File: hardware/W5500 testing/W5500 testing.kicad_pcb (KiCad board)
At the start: 2 copper layers, 34.4 x 53.7 mm, 43 parts, among them J4 Conn_01x08_Pin, J5 RJ45_Amphenol_RJMG1BD3B8K1ANR, Q4 MMBT5550L, Q5 MMBT5550L, U22 W5500, Y1 Crystal_GND24

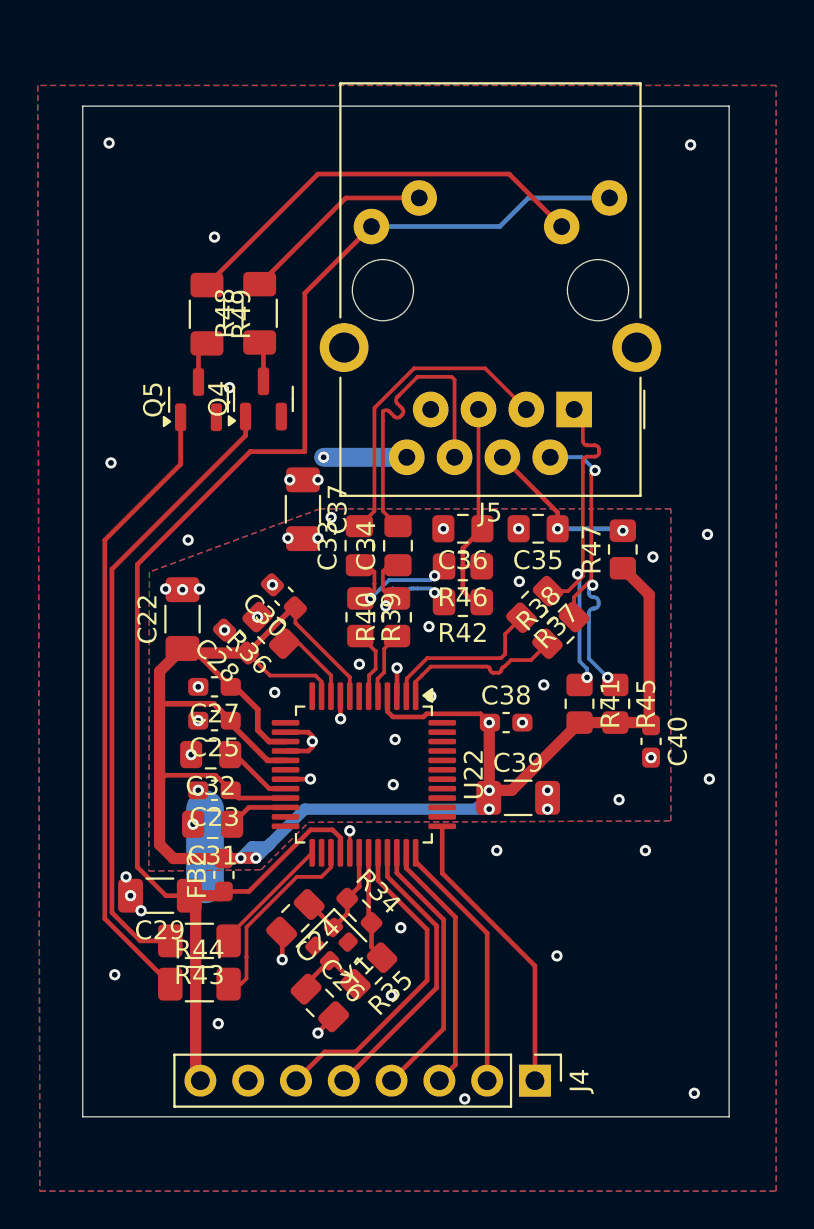
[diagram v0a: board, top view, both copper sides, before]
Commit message: VT interconnect cable specs and w5500 test board
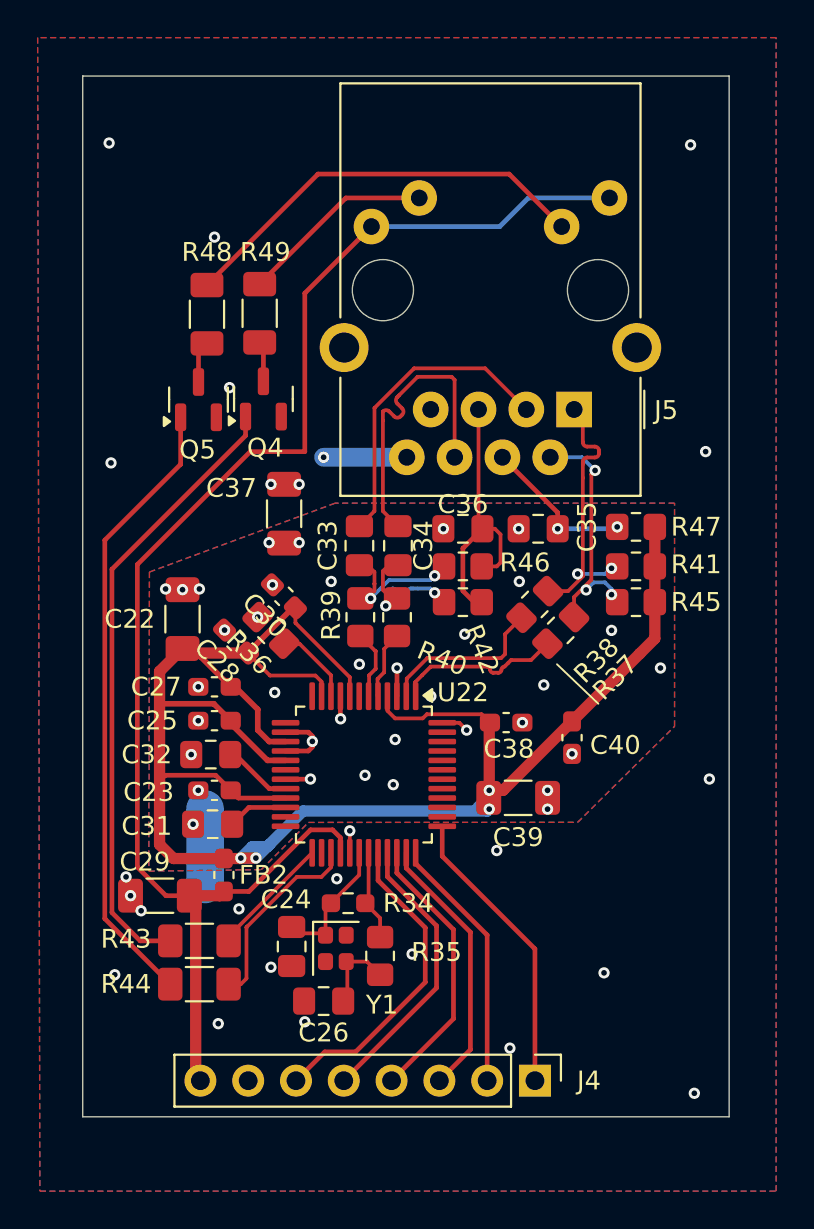
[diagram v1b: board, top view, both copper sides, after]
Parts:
- moved R41 7.89 mm to (134.9, 102.9), turned to 0 degrees
- moved R45 5.51 mm to (134.9, 104.8), turned to 0 degrees
- moved C40 4.20 mm to (131.5, 112.0)
- moved C24 1.51 mm to (116.6, 123.1), turned to -90 degrees
- moved R47 1.39 mm to (134.9, 100.8), turned to 180 degrees
- moved C37 1.03 mm to (116.2, 100.1)
- moved R35 1.00 mm to (121.3, 123.6), turned to -90 degrees
- moved R34 0.72 mm to (119.6, 120.8), turned to 0 degrees
- moved Y1 0.33 mm to (118.9, 123.2), turned to -90 degrees
- moved C26 0.22 mm to (118.3, 126.0), turned to 180 degrees
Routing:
- net /W5500/TD-: track 16.9 -> 12.9 mm
- net /W5500/TD+: track 18.2 -> 14.4 mm
- net /GND: track 8.28 -> 5.59 mm, vias 26 -> 25
- net Net-(J5-RCT): track 12.6 -> 15.1 mm
- net /W5500/AGND: track 7.63 -> 9.09 mm, vias 34 -> 36
- net Net-(U22-XI/CLKIN): track 6.33 -> 7.44 mm
- net Net-(U22-XO): track 5.87 -> 4.88 mm
- net /W5500/MOSI: track 13.5 -> 14.2 mm
- net /W5500/+3.3VA: track 107.5 -> 106.9 mm, vias 5 -> 4
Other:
- board size 34.4 x 53.7 mm -> 34.4 x 55.3 mm

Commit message: joined wizards
wizz chip no more split ground. seems scuffed before, less scuffed
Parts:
- removed NT1: NetTie_2, NetTie:NetTie-2_SMD_Pad2.0mm
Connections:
- C22 pad 2: /W5500/AGND -> /GND
- C23 pad 2: /W5500/AGND -> /GND
- C25 pad 2: /W5500/AGND -> /GND
- C27 pad 2: /W5500/AGND -> /GND
- C28 pad 2: /W5500/AGND -> /GND
- C30 pad 2: /W5500/AGND -> /GND
- C31 pad 2: /W5500/AGND -> /GND
- C32 pad 2: /W5500/AGND -> /GND
- C35 pad 2: /W5500/AGND -> /GND
- C36 pad 2: /W5500/AGND -> /GND
- C37 pad 2: /W5500/AGND -> /GND
- C38 pad 2: /W5500/AGND -> /GND
- C39 pad 2: /W5500/AGND -> /GND
- C40 pad 2: /W5500/AGND -> /GND
- R36 pad 2: /W5500/AGND -> /GND
- U22 pad 14: /W5500/AGND -> /GND
- U22 pad 16: /W5500/AGND -> /GND
- U22 pad 19: /W5500/AGND -> /GND
- U22 pad 3: /W5500/AGND -> /GND
- U22 pad 48: /W5500/AGND -> /GND
- U22 pad 9: /W5500/AGND -> /GND
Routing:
- net /W5500/AGND: track 9.09 -> 0.00 mm, vias 36 -> 0
- net /GND: track 5.59 -> 14.7 mm, vias 25 -> 63
- removed copper zone on B.Cu, net /W5500/AGND
- removed copper zone on F.Cu, net /W5500/AGND

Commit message: mb v1.1 on da way
shuffled around stuff. review notes. made notes. glory to those who look forward and all that fuzz
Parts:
- removed C37: 1n 2kV, Capacitor_SMD:C_1206_3216Metric_Pad1.33x1.80mm_HandSolder
- R35: value 0 -> 14.3
- moved Q5 14.5 mm to (115.8, 80.1)
- moved R49 5.67 mm to (115.8, 85.2), turned to 90 degrees
- moved Q4 2.40 mm to (115.8, 96.3)
- moved R48 2.06 mm to (115.8, 91.3)
- turned R35 to 90 degrees
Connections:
- R35 pad 1: Net-(U22-XO) -> Net-(C26-Pad1)
- R35 pad 2: Net-(C26-Pad1) -> Net-(U22-XO)
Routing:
- net Net-(Q5-B): track 33.2 -> 49.4 mm
- net Net-(J5-PadL3): track 22.5 -> 18.8 mm
- net Net-(Q5-C): track 2.24 -> 4.49 mm
- net Net-(Q4-B): track 33.0 -> 32.0 mm
- net Net-(J5-PadL2): track 10.4 -> 11.3 mm
- net /GND: vias 63 -> 60

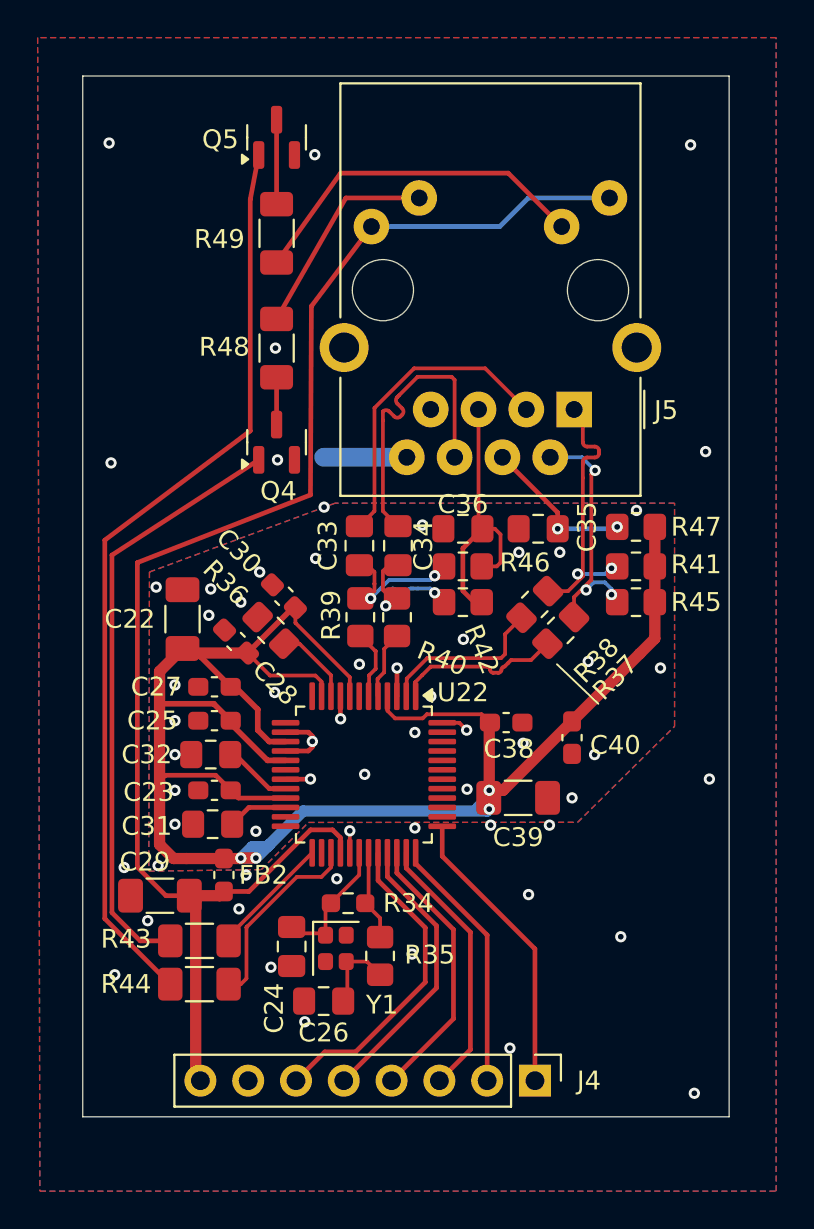
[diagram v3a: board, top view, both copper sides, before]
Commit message: buhhhh
the wizzard is back. help. decimated the totem pole optocoupler symbol , some pins were where they werent supposed to be
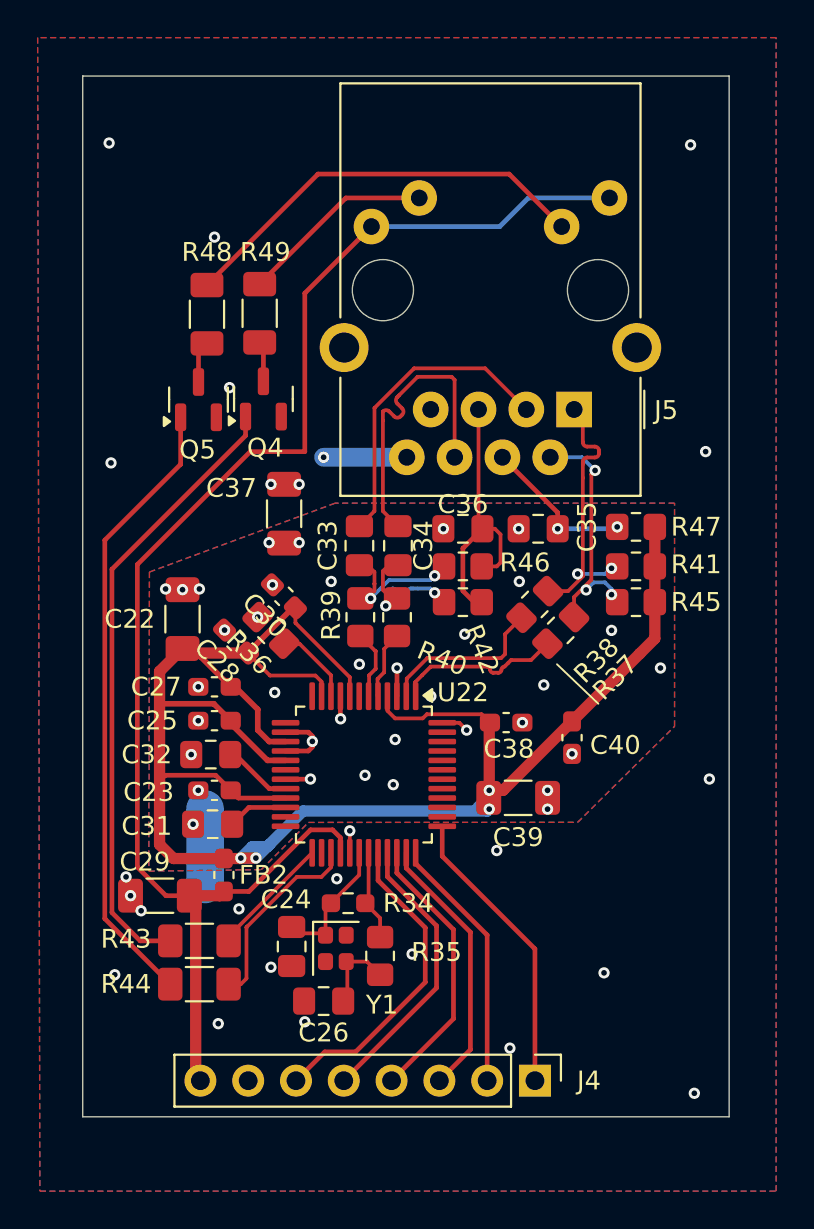
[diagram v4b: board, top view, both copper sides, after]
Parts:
- added C37: 1n 2kV, Capacitor_SMD:C_1206_3216Metric_Pad1.33x1.80mm_HandSolder, F.Cu at (116.2, 100.1)
- added NT1: NetTie_2, NetTie:NetTie-2_SMD_Pad2.0mm, B.Cu at (112.0, 117.8)
- R35: value 14.3 -> 0
- moved Q5 14.5 mm to (111.7, 94.0)
- moved R49 5.67 mm to (112.1, 89.5), turned to -90 degrees
- moved Q4 2.40 mm to (115.1, 94.0)
- moved R48 2.06 mm to (114.9, 89.5)
- turned R35 to -90 degrees
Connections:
- C22 pad 2: /GND -> /W5500/AGND
- C23 pad 2: /GND -> /W5500/AGND
- C25 pad 2: /GND -> /W5500/AGND
- C27 pad 2: /GND -> /W5500/AGND
- C28 pad 2: /GND -> /W5500/AGND
- C30 pad 2: /GND -> /W5500/AGND
- C31 pad 2: /GND -> /W5500/AGND
- C32 pad 2: /GND -> /W5500/AGND
- C35 pad 2: /GND -> /W5500/AGND
- C36 pad 2: /GND -> /W5500/AGND
- C38 pad 2: /GND -> /W5500/AGND
- C39 pad 2: /GND -> /W5500/AGND
- C40 pad 2: /GND -> /W5500/AGND
- R35 pad 1: Net-(C26-Pad1) -> Net-(U22-XO)
- R35 pad 2: Net-(U22-XO) -> Net-(C26-Pad1)
- R36 pad 2: /GND -> /W5500/AGND
- U22 pad 14: /GND -> /W5500/AGND
- U22 pad 16: /GND -> /W5500/AGND
- U22 pad 19: /GND -> /W5500/AGND
- U22 pad 3: /GND -> /W5500/AGND
- U22 pad 48: /GND -> /W5500/AGND
- U22 pad 9: /GND -> /W5500/AGND
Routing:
- net Net-(Q5-B): track 49.4 -> 33.2 mm
- net /W5500/AGND: track 0.00 -> 9.09 mm, vias 0 -> 36
- net /GND: track 14.7 -> 5.59 mm, vias 60 -> 25
- net Net-(J5-PadL3): track 18.8 -> 22.5 mm
- net Net-(Q5-C): track 4.49 -> 2.24 mm
- net Net-(Q4-B): track 32.0 -> 33.0 mm
- net Net-(J5-PadL2): track 11.3 -> 10.4 mm
- added copper zone on B.Cu, net /W5500/AGND
- added copper zone on F.Cu, net /W5500/AGND
